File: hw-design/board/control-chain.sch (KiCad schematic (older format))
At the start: 37 parts, among them J1 RJ45_LEDS, J2 RJ45_LEDS, Q1 MMBT3904, Q2 MMBT3904, Q3 MMBT3904, Q4 MMBT3904, Q5 MMBT3906, U3 MAX13450E

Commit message: sch: control chain circuit (wip)
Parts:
- added C? (x2): 100nF X7R, Capacitors_SMD:C_0603, symbol C
- added D? (x2): D, symbol D
- added J?: CC_INPUT, MOD_Footprints:RJ45-RJHSE5084, symbol RJ45_LEDS
- added J?: CC_OUTPUT, MOD_Footprints:RJ45-RJHSE5084, symbol RJ45_LEDS
- added Q?: RFML8244TRPBF, symbol Q_NMOS_GSD
- added Q?: 2N7002, symbol Q_NMOS_GSD
- added R? (x2): 10k, Resistors_SMD:R_0603, symbol R
- added R?: 100R, symbol R
- added R?: 5k6, symbol R
- added R?: 3k3, symbol R
- added U?: ISL83491, symbol ISL83491
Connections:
- net +3V3: now also U?.13 (VCC), U?.14 (VCC)
- net GNDD: now also C?.2, C?.2, J?.7, J?.8, J?.8, Q?.2 (S), R?.1, R?.2, U?.6 (GND), U?.7 (GND)
- net RS422_RX+: now also J?.1, J?.3, Q?.3 (D), U?.12 (A)
- net RS422_RX-: now also J?.2, J?.6, R?.2, U?.11 (~B)
- net RS422_TX+: now also J?.1, J?.3, U?.9 (Y)
- net RS422_TX-: now also J?.2, J?.6, U?.10 (~Z~)
- net RX_CHAIN: now also U?.2 (RO)
- net TX_CHAIN: now also U?.5 (DI)
- new net: D?.2 (A), J?.5
- new net: D?.1 (K), J?.7
- new net: Q?.3 (D), U?.3 (~RE)
- new net: R?.2, R?.2, U?.4 (DE)
- new net: Q?.2 (S), R?.1
- new net +9V: J?.4, J?.4, J?.5, R?.1
- new net CC_INPUT_DET: C?.1, D?.1 (K), Q?.1 (G), R?.1, R?.1
- new net CC_OUTPUT_DET: C?.1, D?.2 (A), Q?.1 (G), R?.2
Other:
- note added: "TERMINATION RESISTOR"
- moved on the sheet: C10, C11, C7, C8, C9, D2, D3, J1, J2, Q1, Q2, Q3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

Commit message: sch: control chain circuit
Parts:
- removed C10, C11, C7, C?: 100nF X7R, Capacitors_SMD:C_0603, symbol C
- removed C8, C9: 100uF, Capacitors_ThroughHole:Capacitor5x6RM2.5, symbol CP1
- removed D2, D3: MMSZ5242B, Diodes_SMD:SOD-123, symbol ZENERsmall
- removed D?: D, symbol D
- removed J1, J2: RJ45_LEDS, MOD_Footprints:RJ45-RJHSE5084, symbol RJ45_LEDS
- removed Q1, Q2, Q3, Q4: MMBT3904, Transistors_SMD:sot23, symbol MMBT3904
- removed Q5: MMBT3906, Transistors_SMD:sot23, symbol MMBT3906
- removed Q?: 2N7002, symbol Q_NMOS_GSD
- removed R1, R10, R13, R17, R18, R2, R20, R22, R7, R?: 10k, Resistors_SMD:R_0603, symbol R
- removed R11: 0R/NC, Resistors_SMD:R_0603, symbol R
- removed R12, R14, R15, R16, R19: 100k, Resistors_SMD:R_0603, symbol R
- removed R21: 1k, Resistors_SMD:R_0603, symbol R
- removed R3, R4, R5, R6: 1K2, Resistors_SMD:R_0603, symbol R
- removed R8, R9: 100R 0.5W, Resistors_SMD:R_1210, symbol R
- removed R?: 5k6, symbol R
- removed U3: MAX13450E, Housings_SSOP:TSSOP-14_4.4x5mm_Pitch0.65mm, symbol MAX13450E
- added Q? (x2): 2N7002, symbol Q_NMOS_GSD
- added R? (x4): 1k, symbol R
- added R? (x3): 10k, symbol R
- D?: value D -> 1N4148
- R?: value 3k3 -> 10k
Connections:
- net +3V3: now also R?.2
- net +9V: now also R?.2, R?.2, R?.2, R?.2, R?.2, R?.2
- net GNDD: now also Q?.2 (S), Q?.2 (S)
- net at J?.10: now also R?.1 (x2)
- net RS485_RX_LED: now reaches J?.11
- net RS485_RX_LED: now also J?.11, Q?.3 (D), R?.1
- net at J?.12: now also R?.1 (x2)
- net POWER_INPUT: now reaches J?.5
- net RS485_TX_LED: now reaches J?.9
- net RS485_TX_LED: now also J?.9, Q?.3 (D), R?.1
- net CHAIN_RE: now reaches U?.3 (~RE)
- net CHAIN_RE: now also R?.1
- net CHAIN_DE: now reaches R?.2, U?.4 (DE)
- net RS422_RX+ renamed RS485_RX+
- net RS422_RX- renamed RS485_RX-
- net RS422_TX+ renamed RS485_TX+
- net RS422_TX- renamed RS485_TX-
- net RX_CHAIN renamed CHAIN_RX
- net TX_CHAIN renamed CHAIN_TX
- new net RX_LED: Q?.1 (G)
- new net TX_LED: Q?.1 (G)
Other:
- note added: "CONNECTORS"
- note added: "INTERFACE"
- note added: "STATUS LEDS"
- note removed: "PCB consideration: \nThis capacitor must \nbe placed as close as \npossible to the IC"
- moved on the sheet: C?, D?, J?, Q?, R?, U?

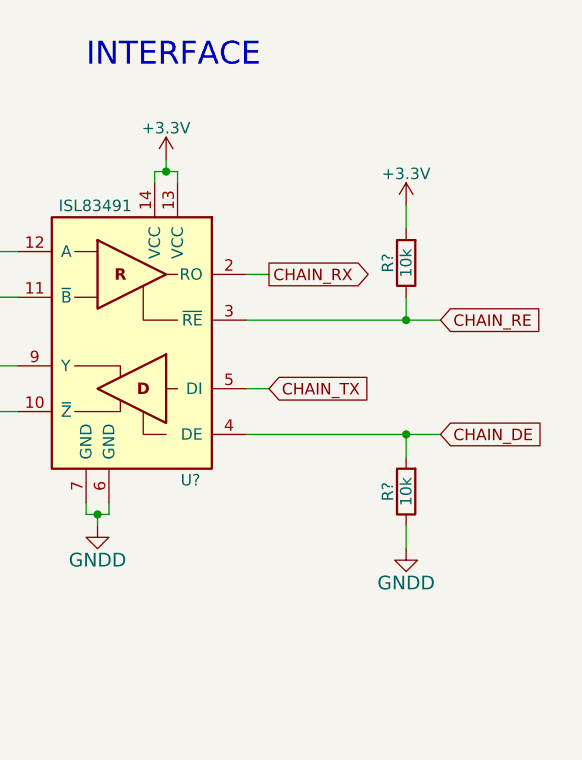
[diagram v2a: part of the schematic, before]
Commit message: sch: cpu, I/Os and control chain circuits done
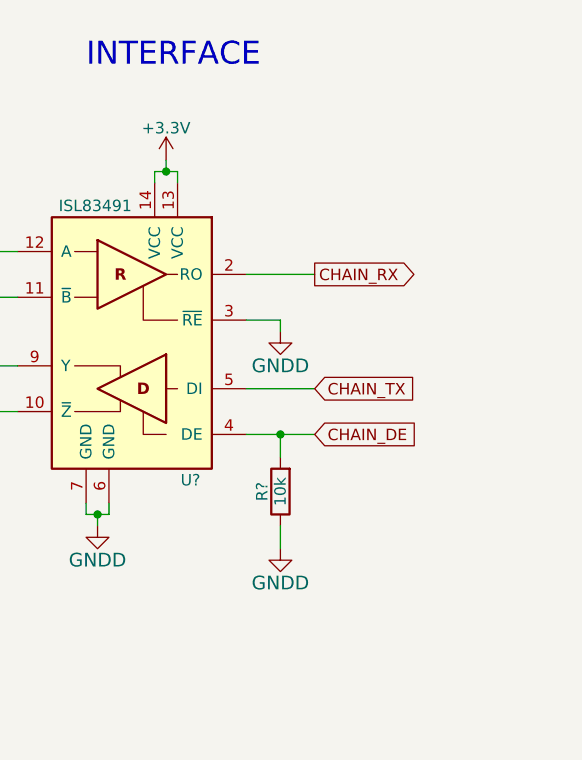
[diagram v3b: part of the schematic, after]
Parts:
- removed R?: 10k, symbol R
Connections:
- net CHAIN_RE is gone; now on net GNDD: U?.3 (~RE)
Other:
- moved on the sheet: R?
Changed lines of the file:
@@
 Connection ~ 8150 1650
 Wire Wire Line
-	8500 2800 9200 2800
-Wire Wire Line
-	9200 2800 9350 2800
+	8500 2800 8650 2800
+Wire Wire Line
+	8650 2800 8800 2800
 $Comp
 L R R?
 U 1 1 557DF2C0
-P 9200 3050
-F 0 "R?" V 9280 3050 50  0000 C CNN
-F 1 "10k" V 9200 3050 50  0000 C CNN
-F 2 "" V 9130 3050 30  0000 C CNN
-F 3 "" H 9200 3050 30  0000 C CNN
-	1    9200 3050
+P 8650 3050
+F 0 "R?" V 8730 3050 50  0000 C CNN
+F 1 "10k" V 8650 3050 50  0000 C CNN
+F 2 "" V 8580 3050 30  0000 C CNN
+F 3 "" H 8650 3050 30  0000 C CNN
+	1    8650 3050
 	-1   0    0    1
 $EndComp
 Wire Wire Line
-	9200 2900 9200 2800
-Connection ~ 9200 2800
+	8650 2900 8650 2800
+Connection ~ 8650 2800
 $Comp
 L GNDD #PWR?
 U 1 1 557DFB58
-P 9200 3300
-F 0 "#PWR?" H 9200 3050 60  0001 C CNN
-F 1 "GNDD" H 9200 3150 60  0000 C CNN
-F 2 "" H 9200 3300 60  0000 C CNN
-F 3 "" H 9200 3300 60  0000 C CNN
-	1    9200 3300
-	1    0    0    -1
-$EndComp
-Wire Wire Line
-	9200 3300 9200 3200
-Text GLabel 8600 2600 2    50   Input ~ 0
+P 8650 3300
+F 0 "#PWR?" H 8650 3050 60  0001 C CNN
+F 1 "GNDD" H 8650 3150 60  0000 C CNN
+F 2 "" H 8650 3300 60  0000 C CNN
+F 3 "" H 8650 3300 60  0000 C CNN
+	1    8650 3300
+	1    0    0    -1
+$EndComp
+Wire Wire Line
+	8650 3300 8650 3200
+Text GLabel 8800 2600 2    50   Input ~ 0
 CHAIN_TX
-Text GLabel 8600 2100 2    50   Output ~ 0
+Text GLabel 8800 2100 2    50   Output ~ 0
 CHAIN_RX
 Wire Wire Line
-	8500 2100 8600 2100
-Wire Wire Line
-	8600 2600 8500 2600
+	8500 2100 8800 2100
+Wire Wire Line
+	8800 2600 8500 2600
 $Comp
 L R R?
@@
 Wire Wire Line
 	2000 6600 2150 6600
-Text GLabel 9350 2800 2    50   Input ~ 0
+Text GLabel 8800 2800 2    50   Input ~ 0
 CHAIN_DE
-$Comp
-L R R?
-U 1 1 557ABC66
-P 9200 2050
-F 0 "R?" V 9280 2050 50  0000 C CNN
-F 1 "10k" V 9200 2050 50  0000 C CNN
-F 2 "" V 9130 2050 30  0000 C CNN
-F 3 "" H 9200 2050 30  0000 C CNN
-	1    9200 2050
-	-1   0    0    1
-$EndComp
-Text GLabel 9350 2300 2    50   Input ~ 0
-CHAIN_RE
-Wire Wire Line
-	8500 2300 9200 2300
-Wire Wire Line
-	9200 2300 9350 2300
-Wire Wire Line
-	9200 2200 9200 2300
-Connection ~ 9200 2300
-$Comp
-L +3.3V #PWR?
-U 1 1 557ACC05
-P 9200 1800
-F 0 "#PWR?" H 9200 1650 50  0001 C CNN
-F 1 "+3.3V" H 9200 1940 50  0000 C CNN
-F 2 "" H 9200 1800 60  0000 C CNN
-F 3 "" H 9200 1800 60  0000 C CNN
-	1    9200 1800
-	1    0    0    -1
-$EndComp
-Wire Wire Line
-	9200 1900 9200 1800
 $Comp
 L Q_NMOS_GSD Q?
@@
 Text Notes 7800 1200 0    100  ~ 0
 INTERFACE
+$Comp
+L GNDD #PWR?
+U 1 1 557F118D
+P 8650 2350
+F 0 "#PWR?" H 8650 2100 60  0001 C CNN
+F 1 "GNDD" H 8650 2200 60  0000 C CNN
+F 2 "" H 8650 2350 60  0000 C CNN
+F 3 "" H 8650 2350 60  0000 C CNN
+	1    8650 2350
+	1    0    0    -1
+$EndComp
+Wire Wire Line
+	8500 2300 8650 2300
+Wire Wire Line
+	8650 2300 8650 2350
 $EndSCHEMATC

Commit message: sch: schematic annotation done
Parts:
- gave numbers to parts that had none: 17
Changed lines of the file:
@@
 $EndDescr
 $Comp
-L RJ45_LEDS J?
+L RJ45_LEDS J1
 U 1 1 55788CDD
 P 3150 2000
-F 0 "J?" H 3150 1500 50  0000 C CNN
+F 0 "J1" H 3150 1500 50  0000 C CNN
 F 1 "CC_INPUT" H 3150 2400 50  0000 C CNN
 F 2 "MOD_Footprints:RJ45-RJHSE5084" H 3150 1950 60  0001 C CNN
@@
 RS485_RX-
 $Comp
-L RJ45_LEDS J?
+L RJ45_LEDS J2
 U 1 1 5578CA2C
 P 3150 3800
-F 0 "J?" H 3150 3300 50  0000 C CNN
+F 0 "J2" H 3150 3300 50  0000 C CNN
 F 1 "CC_OUTPUT" H 3150 4200 50  0000 C CNN
 F 2 "MOD_Footprints:RJ45-RJHSE5084" H 3150 3750 60  0001 C CNN
@@
 RS485_RX-
 $Comp
-L GNDD #PWR?
+L GNDD #PWR022
 U 1 1 557962A0
 P 3750 2500
-F 0 "#PWR?" H 3750 2250 60  0001 C CNN
+F 0 "#PWR022" H 3750 2250 60  0001 C CNN
 F 1 "GNDD" H 3750 2350 60  0000 C CNN
 F 2 "" H 3750 2500 60  0000 C CNN
@@
 $EndComp
 $Comp
-L GNDD #PWR?
+L GNDD #PWR023
 U 1 1 55797530
 P 3750 4300
-F 0 "#PWR?" H 3750 4050 60  0001 C CNN
+F 0 "#PWR023" H 3750 4050 60  0001 C CNN
 F 1 "GNDD" H 3750 4150 60  0000 C CNN
 F 2 "" H 3750 4300 60  0000 C CNN
@@
 POWER_INPUT
 $Comp
-L ISL83491 U?
+L ISL83491 U3
 U 1 1 557A059C
 P 8000 2400
-F 0 "U?" H 7700 1800 50  0000 L CNN
+F 0 "U3" H 7700 1800 50  0000 L CNN
 F 1 "ISL83491" H 8000 3000 50  0000 L CNN
 F 2 "" H 8000 2400 50  0001 C CIN
@@
 CC_OUTPUT_DET
 $Comp
-L C C?
+L C C9
 U 1 1 557A7843
 P 4950 4400
-F 0 "C?" V 4800 4400 40  0000 L CNN
+F 0 "C9" V 4800 4400 40  0000 L CNN
 F 1 "100nF X7R" V 5100 4250 40  0000 L CNN
 F 2 "Capacitors_SMD:C_0603" H 4988 4250 30  0001 C CNN
@@
 $EndComp
 $Comp
-L R R?
+L R R11
 U 1 1 557A7849
 P 4950 3800
-F 0 "R?" V 5050 3800 40  0000 C CNN
+F 0 "R11" V 5050 3800 40  0000 C CNN
 F 1 "10k" V 4957 3801 40  0000 C CNN
 F 2 "Resistors_SMD:R_0603" V 4880 3800 30  0001 C CNN
@@
 $EndComp
 $Comp
-L GNDD #PWR?
+L GNDD #PWR024
 U 1 1 557A784F
 P 4950 4650
-F 0 "#PWR?" H 4950 4400 60  0001 C CNN
+F 0 "#PWR024" H 4950 4400 60  0001 C CNN
 F 1 "GNDD" H 4950 4500 60  0000 C CNN
 F 2 "" H 4950 4650 60  0000 C CNN
@@
 $EndComp
 $Comp
-L +9V #PWR?
+L +9V #PWR025
 U 1 1 557AE435
 P 4950 3550
-F 0 "#PWR?" H 4950 3400 50  0001 C CNN
+F 0 "#PWR025" H 4950 3400 50  0001 C CNN
 F 1 "+9V" H 4950 3690 50  0000 C CNN
 F 2 "" H 4950 3550 60  0000 C CNN
@@
 $EndComp
 $Comp
-L +9V #PWR?
+L +9V #PWR026
 U 1 1 557B6A6D
 P 4400 3550
-F 0 "#PWR?" H 4400 3400 50  0001 C CNN
+F 0 "#PWR026" H 4400 3400 50  0001 C CNN
 F 1 "+9V" H 4400 3690 50  0000 C CNN
 F 2 "" H 4400 3550 60  0000 C CNN
@@
 $EndComp
 $Comp
-L +9V #PWR?
+L +9V #PWR027
 U 1 1 557B80CC
 P 4400 1750
-F 0 "#PWR?" H 4400 1600 50  0001 C CNN
+F 0 "#PWR027" H 4400 1600 50  0001 C CNN
 F 1 "+9V" H 4400 1890 50  0000 C CNN
 F 2 "" H 4400 1750 60  0000 C CNN
@@
 $EndComp
 $Comp
-L Q_NMOS_GSD Q?
+L Q_NMOS_GSD Q6
 U 1 1 557BCC32
 P 8200 4950
-F 0 "Q?" H 8100 5050 50  0000 R CNN
+F 0 "Q6" H 8100 5050 50  0000 R CNN
 F 1 "RFML8244TRPBF" V 8450 5200 50  0000 R CNN
 F 2 "" H 8400 5050 29  0000 C CNN
@@
 $EndComp
 $Comp
-L R R?
+L R R12
 U 1 1 557BF829
 P 8300 5400
-F 0 "R?" V 8380 5400 50  0000 C CNN
+F 0 "R12" V 8380 5400 50  0000 C CNN
 F 1 "100R" V 8300 5400 50  0000 C CNN
 F 2 "" V 8230 5400 30  0000 C CNN
@@
 $EndComp
 $Comp
-L D D?
+L D D4
 U 1 1 557C221B
 P 4550 4100
-F 0 "D?" H 4550 4200 50  0000 C CNN
+F 0 "D4" H 4550 4200 50  0000 C CNN
 F 1 "1N4148" H 4550 4000 50  0000 C CNN
 F 2 "" H 4550 4100 60  0000 C CNN
@@
 	3650 2300 3750 2300
 Wire Wire Line
-	3750 2300 3750 2400
-Wire Wire Line
-	3750 2400 3750 2500
+	3750 2300 3750 2500
 Wire Wire Line
 	3650 2400 3750 2400
@@
 	4950 4550 4950 4650
 Wire Wire Line
-	4700 4100 4950 4100
-Wire Wire Line
-	4950 4100 5300 4100
-Wire Wire Line
-	4950 3950 4950 4100
-Wire Wire Line
-	4950 4100 4950 4250
+	4700 4100 5300 4100
+Wire Wire Line
+	4950 3950 4950 4250
 Connection ~ 4950 4100
 Wire Wire Line
 	4950 3650 4950 3550
 Wire Wire Line
-	3650 3700 3750 3700
-Wire Wire Line
-	3750 3700 4400 3700
+	3650 3700 4400 3700
 Wire Wire Line
 	4400 3700 4400 3550
@@
 	7800 4950 8000 4950
 $Comp
-L GNDD #PWR?
+L GNDD #PWR028
 U 1 1 557D6D91
 P 7850 3200
-F 0 "#PWR?" H 7850 2950 60  0001 C CNN
+F 0 "#PWR028" H 7850 2950 60  0001 C CNN
 F 1 "GNDD" H 7850 3050 60  0000 C CNN
 F 2 "" H 7850 3200 60  0000 C CNN
@@
 	7800 3100 7800 3150
 Wire Wire Line
-	7800 3150 7850 3150
-Wire Wire Line
-	7850 3150 7900 3150
+	7800 3150 7900 3150
 Wire Wire Line
 	7900 3150 7900 3100
@@
 Connection ~ 7850 3150
 $Comp
-L +3.3V #PWR?
+L +3.3V #PWR029
 U 1 1 557D9E83
 P 8150 1600
-F 0 "#PWR?" H 8150 1450 50  0001 C CNN
+F 0 "#PWR029" H 8150 1450 50  0001 C CNN
 F 1 "+3.3V" H 8150 1740 50  0000 C CNN
 F 2 "" H 8150 1600 60  0000 C CNN
@@
 	8100 1700 8100 1650
 Wire Wire Line
-	8100 1650 8150 1650
-Wire Wire Line
-	8150 1650 8200 1650
+	8100 1650 8200 1650
 Wire Wire Line
 	8200 1650 8200 1700
@@
 Connection ~ 8150 1650
 Wire Wire Line
-	8500 2800 8650 2800
-Wire Wire Line
-	8650 2800 8800 2800
-$Comp
-L R R?
+	8500 2800 8800 2800
+$Comp
+L R R13
 U 1 1 557DF2C0
 P 8650 3050
-F 0 "R?" V 8730 3050 50  0000 C CNN
+F 0 "R13" V 8730 3050 50  0000 C CNN
 F 1 "10k" V 8650 3050 50  0000 C CNN
 F 2 "" V 8580 3050 30  0000 C CNN
@@
 Connection ~ 8650 2800
 $Comp
-L GNDD #PWR?
+L GNDD #PWR030
 U 1 1 557DFB58
 P 8650 3300
-F 0 "#PWR?" H 8650 3050 60  0001 C CNN
+F 0 "#PWR030" H 8650 3050 60  0001 C CNN
 F 1 "GNDD" H 8650 3150 60  0000 C CNN
 F 2 "" H 8650 3300 60  0000 C CNN
@@
 	8800 2600 8500 2600
 $Comp
-L R R?
+L R R7
 U 1 1 557910FB
 P 2400 3400
-F 0 "R?" V 2480 3400 50  0000 C CNN
+F 0 "R7" V 2480 3400 50  0000 C CNN
 F 1 "1k" V 2400 3400 50  0000 C CNN
 F 2 "" V 2330 3400 30  0000 C CNN
@@
 	2250 3400 2150 3400
 $Comp
-L R R?
+L R R5
 U 1 1 5579E2EE
 P 2400 1600
-F 0 "R?" V 2480 1600 50  0000 C CNN
+F 0 "R5" V 2480 1600 50  0000 C CNN
 F 1 "1k" V 2400 1600 50  0000 C CNN
 F 2 "" V 2330 1600 30  0000 C CNN
@@
 	2250 1600 2150 1600
 $Comp
-L R R?
+L R R8
 U 1 1 557A0270
 P 2400 4100
-F 0 "R?" V 2480 4100 50  0000 C CNN
+F 0 "R8" V 2480 4100 50  0000 C CNN
 F 1 "1k" V 2400 4100 50  0000 C CNN
 F 2 "" V 2330 4100 30  0000 C CNN
@@
 	2250 4100 2150 4100
 $Comp
-L R R?
+L R R6
 U 1 1 557A0384
 P 2400 2300
-F 0 "R?" V 2480 2300 50  0000 C CNN
+F 0 "R6" V 2480 2300 50  0000 C CNN
 F 1 "1k" V 2400 2300 50  0000 C CNN
 F 2 "" V 2330 2300 30  0000 C CNN
@@
 STATUS LEDS
 $Comp
-L Q_NMOS_GSD Q?
+L Q_NMOS_GSD Q4
 U 1 1 557A16B1
 P 2350 6600
-F 0 "Q?" H 2250 6650 50  0000 R CNN
+F 0 "Q4" H 2250 6650 50  0000 R CNN
 F 1 "2N7002" V 2550 6750 50  0000 R CNN
 F 2 "" H 2550 6700 29  0000 C CNN
@@
 $EndComp
 $Comp
-L GNDD #PWR?
+L GNDD #PWR031
 U 1 1 557A1AB4
 P 2450 6900
-F 0 "#PWR?" H 2450 6650 60  0001 C CNN
+F 0 "#PWR031" H 2450 6650 60  0001 C CNN
 F 1 "GNDD" H 2450 6750 60  0000 C CNN
 F 2 "" H 2450 6900 60  0000 C CNN
@@
 	2450 6800 2450 6900
 $Comp
-L R R?
+L R R9
 U 1 1 557A2CF3
 P 2450 6050
-F 0 "R?" V 2530 6050 50  0000 C CNN
+F 0 "R9" V 2530 6050 50  0000 C CNN
 F 1 "10k" V 2450 6050 50  0000 C CNN
 F 2 "" V 2380 6050 30  0000 C CNN
@@
 $EndComp
 Wire Wire Line
-	2450 6200 2450 6300
-Wire Wire Line
-	2450 6300 2450 6400
-$Comp
-L +9V #PWR?
+	2450 6200 2450 6400
+$Comp
+L +9V #PWR032
 U 1 1 557A4EDD
 P 2450 5800
-F 0 "#PWR?" H 2450 5650 50  0001 C CNN
+F 0 "#PWR032" H 2450 5650 50  0001 C CNN
 F 1 "+9V" H 2450 5940 50  0000 C CNN
 F 2 "" H 2450 5800 60  0000 C CNN
@@
 CHAIN_DE
 $Comp
-L Q_NMOS_GSD Q?
+L Q_NMOS_GSD Q5
 U 1 1 557B0B85
 P 4200 6600
-F 0 "Q?" H 4100 6650 50  0000 R CNN
+F 0 "Q5" H 4100 6650 50  0000 R CNN
 F 1 "2N7002" V 4400 6750 50  0000 R CNN
 F 2 "" H 4400 6700 29  0000 C CNN
@@
 $EndComp
 $Comp
-L GNDD #PWR?
+L GNDD #PWR033
 U 1 1 557B0B8B
 P 4300 6900
-F 0 "#PWR?" H 4300 6650 60  0001 C CNN
+F 0 "#PWR033" H 4300 6650 60  0001 C CNN
 F 1 "GNDD" H 4300 6750 60  0000 C CNN
 F 2 "" H 4300 6900 60  0000 C CNN
@@
 	4300 6800 4300 6900
 $Comp
-L R R?
+L R R10
 U 1 1 557B0B92
 P 4300 6050
-F 0 "R?" V 4380 6050 50  0000 C CNN
+F 0 "R10" V 4380 6050 50  0000 C CNN
 F 1 "10k" V 4300 6050 50  0000 C CNN
 F 2 "" V 4230 6050 30  0000 C CNN
@@
 $EndComp
 Wire Wire Line
-	4300 6200 4300 6300
-Wire Wire Line
-	4300 6300 4300 6400
-$Comp
-L +9V #PWR?
+	4300 6200 4300 6400
+$Comp
+L +9V #PWR034
 U 1 1 557B0B9A
 P 4300 5800
-F 0 "#PWR?" H 4300 5650 50  0001 C CNN
+F 0 "#PWR034" H 4300 5650 50  0001 C CNN
 F 1 "+9V" H 4300 5940 50  0000 C CNN
 F 2 "" H 4300 5800 60  0000 C CNN
@@
 	3850 6600 4000 6600
 $Comp
-L +9V #PWR?
+L +9V #PWR035
 U 1 1 557B22CB
 P 2150 3300
-F 0 "#PWR?" H 2150 3150 50  0001 C CNN
+F 0 "#PWR035" H 2150 3150 50  0001 C CNN
 F 1 "+9V" H 2150 3440 50  0000 C CNN
 F 2 "" H 2150 3300 60  0000 C CNN
@@
 	2150 3400 2150 3300
 $Comp
-L +9V #PWR?
+L +9V #PWR036
 U 1 1 557B2849
 P 2150 4000
-F 0 "#PWR?" H 2150 3850 50  0001 C CNN
+F 0 "#PWR036" H 2150 3850 50  0001 C CNN
 F 1 "+9V" H 2150 4140 50  0000 C CNN
 F 2 "" H 2150 4000 60  0000 C CNN
@@
 	2150 4100 2150 4000
 $Comp
-L +9V #PWR?
+L +9V #PWR037
 U 1 1 557B3090
 P 2150 2200
-F 0 "#PWR?" H 2150 2050 50  0001 C CNN
+F 0 "#PWR037" H 2150 2050 50  0001 C CNN
 F 1 "+9V" H 2150 2340 50  0000 C CNN
 F 2 "" H 2150 2200 60  0000 C CNN
@@
 	2150 2300 2150 2200
 $Comp
-L +9V #PWR?
+L +9V #PWR038
 U 1 1 557B39CA
 P 2150 1500
-F 0 "#PWR?" H 2150 1350 50  0001 C CNN
+F 0 "#PWR038" H 2150 1350 50  0001 C CNN
 F 1 "+9V" H 2150 1640 50  0000 C CNN
 F 2 "" H 2150 1500 60  0000 C CNN
@@
 INTERFACE
 $Comp
-L GNDD #PWR?
+L GNDD #PWR039
 U 1 1 557F118D
 P 8650 2350
-F 0 "#PWR?" H 8650 2100 60  0001 C CNN
+F 0 "#PWR039" H 8650 2100 60  0001 C CNN
 F 1 "GNDD" H 8650 2200 60  0000 C CNN
 F 2 "" H 8650 2350 60  0000 C CNN
